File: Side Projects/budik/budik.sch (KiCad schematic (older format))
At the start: 77 parts, among them J1 Conn_01x02_Male, J2 USB_OTG, J3 FTDI, Q1 BSS138, SW1 SW_DPST, SW2 SW_DPST, SW3 SW_SPDT, SW4 SW_DPST, SW5 SW_DPST, U1 ESP-12, U2 MCP23018-E_SP, U3 uA7805, U4 LD1117S33CTR

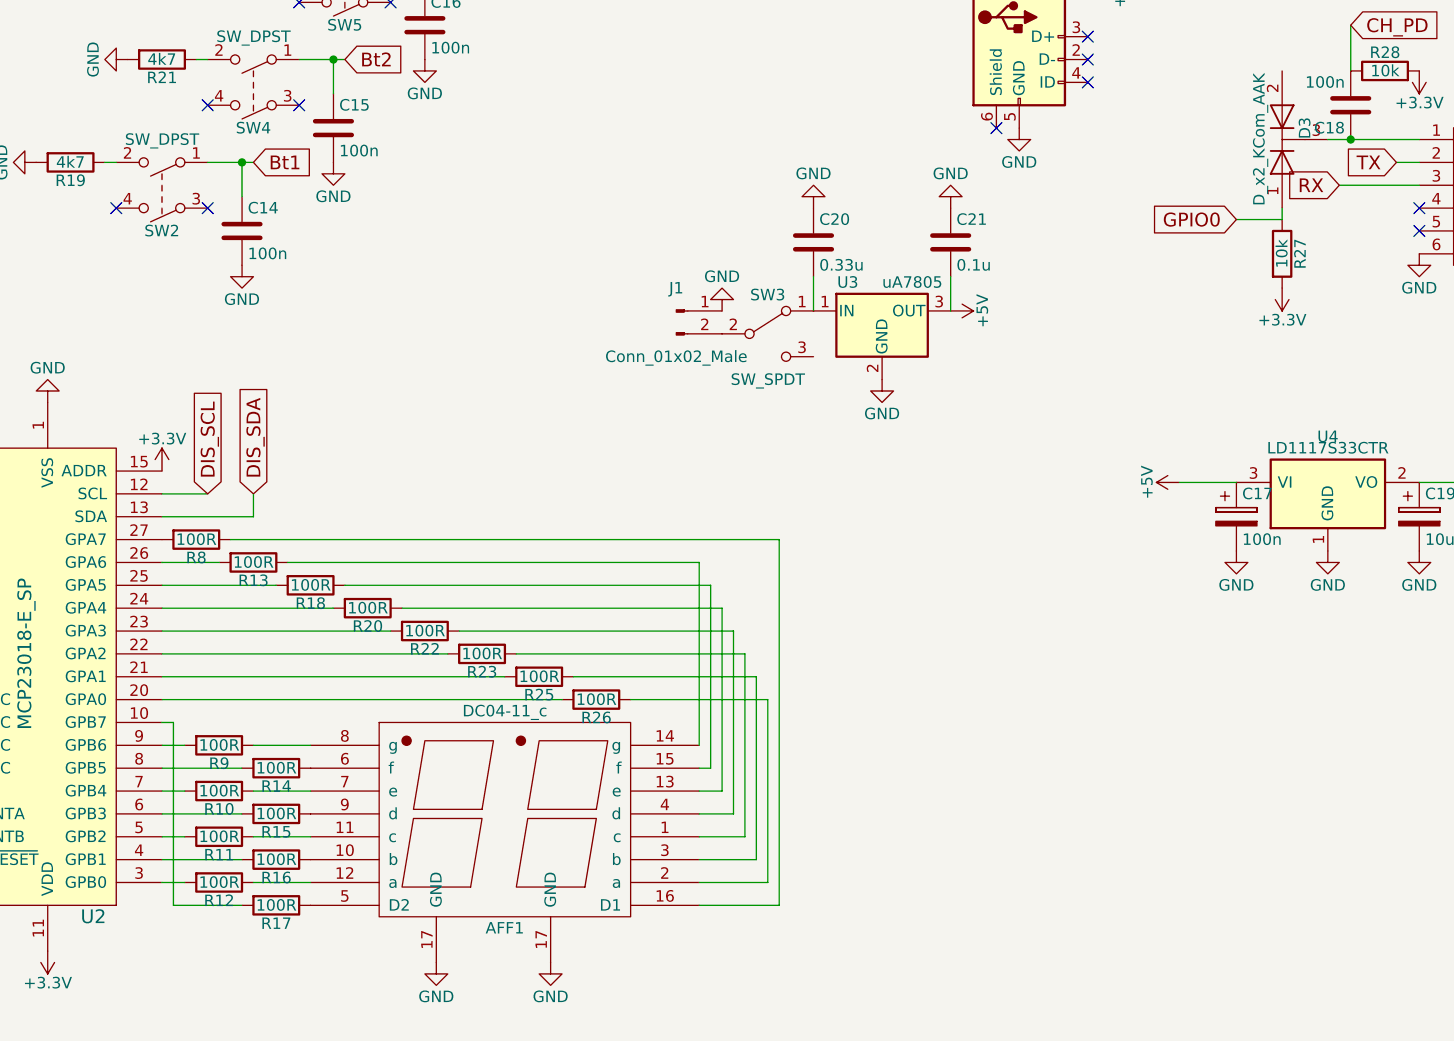
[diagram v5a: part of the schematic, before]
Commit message: Remake PCB into something like square
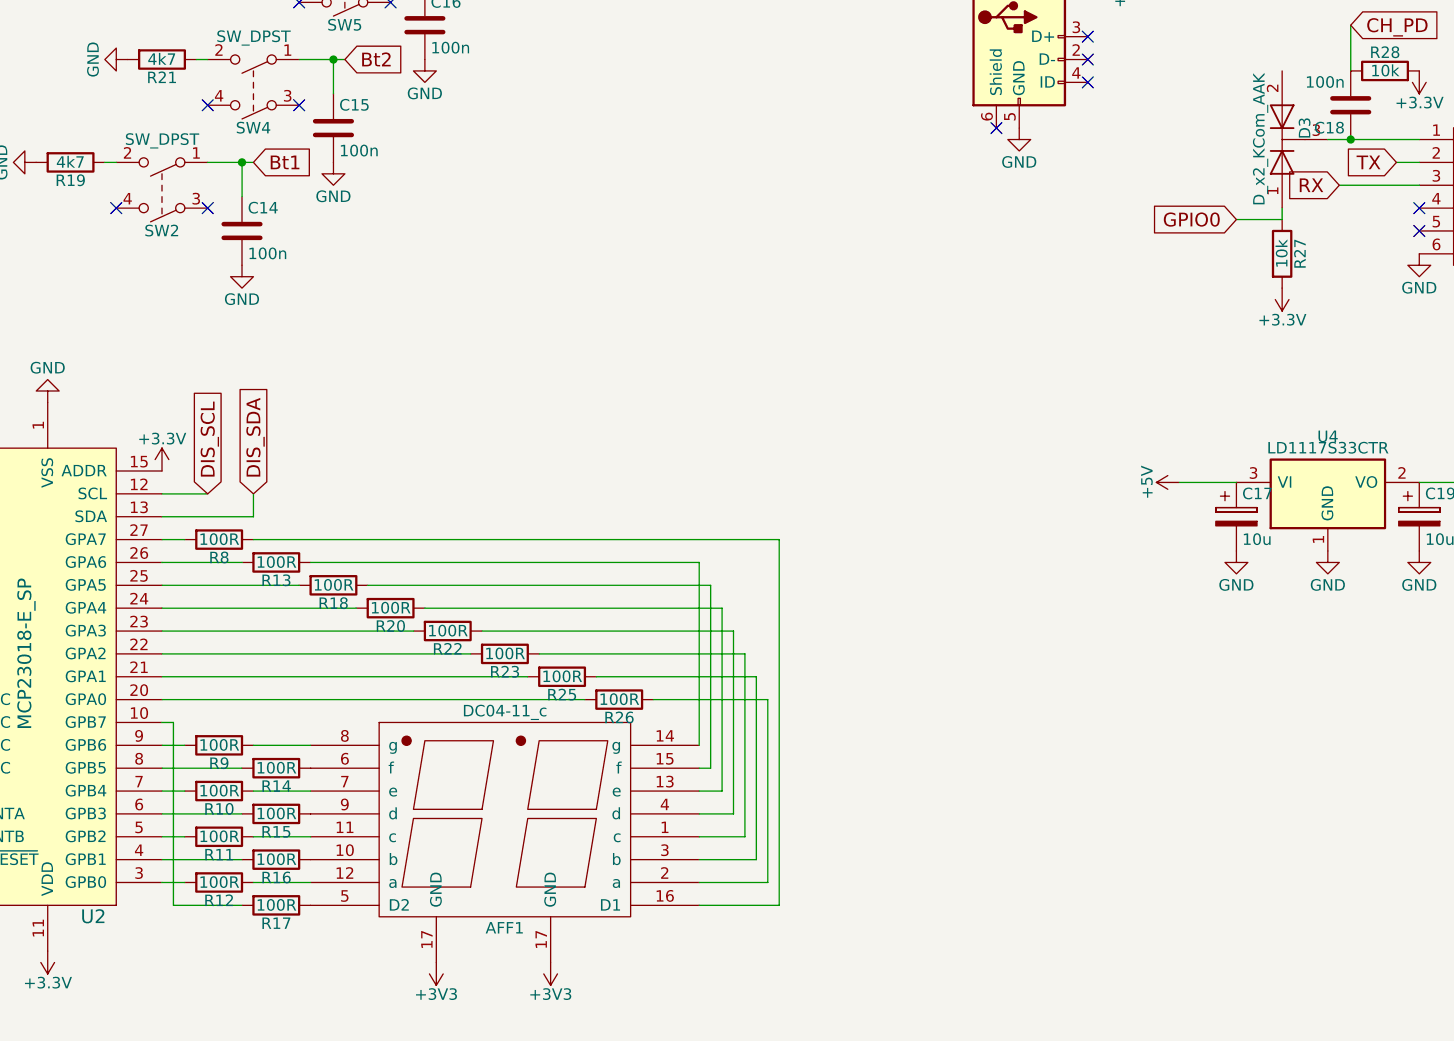
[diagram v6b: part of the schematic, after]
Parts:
- removed C20: 0.33u, Capacitors_SMD:C_0603_HandSoldering, symbol C
- removed C21: 0.1u, Capacitors_SMD:C_0603_HandSoldering, symbol C
- removed J1: Conn_01x02_Male, Pin_Headers:Pin_Header_Angled_1x02_Pitch2.54mm, symbol Conn_01x02_Male
- removed SW3: SW_SPDT, 7_segment:switch, symbol SW_SPDT
- removed U3: uA7805, L7805:78XXS, symbol uA7805
- AFF1: footprint (none) -> Displays_7-Segment:DA56-11CGKWA
- C17: value 100n -> 10u; footprint Capacitors_SMD:CP_Elec_5x5.3 -> Capacitors_Tantalum_SMD:CP_Tantalum_Case-B_EIA-3528-21_Hand
- C19: footprint Capacitors_SMD:CP_Elec_5x5.3 -> Capacitors_Tantalum_SMD:CP_Tantalum_Case-B_EIA-3528-21_Hand
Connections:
- net +3V3: now also AFF1.17 (GND)
- net GND: no longer AFF1.17 (GND)
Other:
- moved on the sheet: R13, R18, R20, R22, R23, R25, R26, R8
